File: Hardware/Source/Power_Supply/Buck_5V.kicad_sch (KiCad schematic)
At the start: 18 parts, among them U8 TPS54331DR

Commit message: update pcb flyback
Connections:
- net GND2: now also U8.7 (GND)
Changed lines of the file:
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@@
+	(wire
+		(pts
+			(xy 120.65 68.58) (xy 120.65 69.85)
+		)
+		(stroke
+			(width 0)
+			(type default)
+		)
+	)
 	(wire
 		(pts
@@
 		(pts
 			(xy 156.21 66.04) (xy 158.75 66.04)
+		)
+		(stroke
+			(width 0)
+			(type default)
+		)
+	)
+	(wire
+		(pts
+			(xy 130.81 68.58) (xy 120.65 68.58)
 		)
 		(stroke
@@
 					(unit 1)
 				)
+			)
+		)
+	)
+	(symbol
+		(lib_id "power:GND2")
+		(at 120.65 69.85 0)
+		(unit 1)
+		(exclude_from_sim no)
+		(in_bom yes)
+		(on_board yes)
+		(dnp no)
+		(fields_autoplaced yes)
+		(property "Reference" "#PWR027"
+			(at 120.65 76.2 0)
+			(effects
+				(font
+					(size 1.27 1.27)
+				)
+				(hide yes)
+			)
+		)
+		(property "Value" "GND2"
+			(at 120.65 74.93 0)
+			(effects
+				(font
+					(size 1.27 1.27)
+				)
+			)
+		)
+		(property "Footprint" ""
+			(at 120.65 69.85 0)
+			(effects
+				(font
+					(size 1.27 1.27)
+				)
+				(hide yes)
+			)
+		)
+		(property "Datasheet" ""
+			(at 120.65 69.85 0)
+			(effects
+				(font
+					(size 1.27 1.27)
+				)
+				(hide yes)
+			)
+		)
+		(property "Description" "Power symbol creates a global label with name \"GND2\" , ground"
+			(at 120.65 69.85 0)
+			(effects
+				(font
+					(size 1.27 1.27)
+				)
+				(hide yes)
+			)
+		)
+		(pin "1"
+		)
+		(instances
+			(project "Power_Supply"
+				(path "/5c8a7907-026b-4416-b231-5ef9f93b99e1/810061e0-77df-407e-a763-7d91437d6cce"
+					(reference "#PWR027")
+					(unit 1)
+				)

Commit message: update de sua sche
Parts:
- renumbered C25 to C45, C26 to C46, C27 to C47, C28 to C48, C29 to C49, C30 to C50, C31 to C51, C32 to C52, D4 to D11, L3 to L4, R19 to R28, R20 to R29, R21 to R30, R15 to R31, R16 to R32, R17 to R33, R18 to R34, U8 to U11
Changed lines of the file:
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@@
 		(on_board yes)
 		(dnp no)
-		(property "Reference" "C30"
+		(property "Reference" "C50"
 			(at 162.56 60.96 0)
 			(effects
@@
 		(pin "1"
 		)
-		(instances
-			(project ""
-				(path "/5c8a7907-026b-4416-b231-5ef9f93b99e1/810061e0-77df-407e-a763-7d91437d6cce"
-					(reference "C30")
-					(unit 1)
-				)
-			)
-		)
+		(instances)
 	)
 	(symbol
@@
 		(on_board yes)
 		(dnp no)
-		(property "Reference" "C32"
+		(property "Reference" "C52"
 			(at 220.726 77.47 90)
 			(effects
@@
 		(pin "2"
 		)
-		(instances
-			(project ""
-				(path "/5c8a7907-026b-4416-b231-5ef9f93b99e1/810061e0-77df-407e-a763-7d91437d6cce"
-					(reference "C32")
-					(unit 1)
-				)
-			)
-		)
+		(instances)
 	)
 	(symbol
@@
 		(on_board yes)
 		(dnp no)
-		(property "Reference" "C28"
+		(property "Reference" "C48"
 			(at 126.492 89.662 90)
 			(effects
@@
 		(pin "1"
 		)
-		(instances
-			(project ""
-				(path "/5c8a7907-026b-4416-b231-5ef9f93b99e1/810061e0-77df-407e-a763-7d91437d6cce"
-					(reference "C28")
-					(unit 1)
-				)
-			)
-		)
+		(instances)
 	)
 	(symbol
@@
 		(dnp no)
 		(fields_autoplaced yes)
-		(property "Reference" "U8"
+		(property "Reference" "U11"
 			(at 143.51 58.42 0)
 			(effects
@@
 		(pin "1"
 		)
-		(instances
-			(project ""
-				(path "/5c8a7907-026b-4416-b231-5ef9f93b99e1/810061e0-77df-407e-a763-7d91437d6cce"
-					(reference "U8")
-					(unit 1)
-				)
-			)
-		)
+		(instances)
 	)
 	(symbol
@@
 		(on_board yes)
 		(dnp no)
-		(property "Reference" "R21"
+		(property "Reference" "R30"
 			(at 106.934 94.996 90)
 			(effects
@@
 		(pin "2"
 		)
-		(instances
-			(project ""
-				(path "/5c8a7907-026b-4416-b231-5ef9f93b99e1/810061e0-77df-407e-a763-7d91437d6cce"
-					(reference "R21")
-					(unit 1)
-				)
-			)
-		)
+		(instances)
 	)
 	(symbol
@@
 		(on_board yes)
 		(dnp no)
-		(property "Reference" "R15"
+		(property "Reference" "R31"
 			(at 239.268 76.454 90)
 			(effects
@@
 		(pin "1"
 		)
-		(instances
-			(project ""
-				(path "/5c8a7907-026b-4416-b231-5ef9f93b99e1/810061e0-77df-407e-a763-7d91437d6cce"
-					(reference "R15")
-					(unit 1)
-				)
-			)
-		)
+		(instances)
 	)
 	(symbol
@@
 		(on_board yes)
 		(dnp no)
-		(property "Reference" "D4"
+		(property "Reference" "D11"
 			(at 172.466 76.708 90)
 			(effects
@@
 		(pin "1"
 		)
-		(instances
-			(project ""
-				(path "/5c8a7907-026b-4416-b231-5ef9f93b99e1/810061e0-77df-407e-a763-7d91437d6cce"
-					(reference "D4")
-					(unit 1)
-				)
-			)
-		)
+		(instances)
 	)
 	(symbol
@@
 		(on_board yes)
 		(dnp no)
-		(property "Reference" "C26"
+		(property "Reference" "C46"
 			(at 67.056 68.58 90)
 			(effects
@@
 		(pin "1"
 		)
-		(instances
-			(project ""
-				(path "/5c8a7907-026b-4416-b231-5ef9f93b99e1/810061e0-77df-407e-a763-7d91437d6cce"
-					(reference "C26")
-					(unit 1)
-				)
-			)
-		)
+		(instances)
 	)
 	(symbol
@@
 		(on_board yes)
 		(dnp no)
-		(property "Reference" "L3"
+		(property "Reference" "L4"
 			(at 182.88 66.04 0)
 			(effects
@@
 		(pin "2"
 		)
-		(instances
-			(project ""
-				(path "/5c8a7907-026b-4416-b231-5ef9f93b99e1/810061e0-77df-407e-a763-7d91437d6cce"
-					(reference "L3")
-					(unit 1)
-				)
-			)
-		)
+		(instances)
 	)
 	(symbol
@@
 		(on_board yes)
 		(dnp no)
-		(property "Reference" "C29"
+		(property "Reference" "C49"
 			(at 143.002 86.614 90)
 			(effects
@@
 		(pin "1"
 		)
-		(instances
-			(project ""
-				(path "/5c8a7907-026b-4416-b231-5ef9f93b99e1/810061e0-77df-407e-a763-7d91437d6cce"
-					(reference "C29")
-					(unit 1)
-				)
-			)
-		)
+		(instances)
 	)
 	(symbol
@@
 		(on_board yes)
 		(dnp no)
-		(property "Reference" "C31"
+		(property "Reference" "C51"
 			(at 201.93 77.47 90)
 			(effects
@@
 		(pin "2"
 		)
-		(instances
-			(project ""
-				(path "/5c8a7907-026b-4416-b231-5ef9f93b99e1/810061e0-77df-407e-a763-7d91437d6cce"
-					(reference "C31")
-					(unit 1)
-				)
-			)
-		)
+		(instances)
 	)
 	(symbol
@@
 		(on_board yes)
 		(dnp no)
-		(property "Reference" "R17"
+		(property "Reference" "R33"
 			(at 239.014 99.06 90)
 			(effects
@@
 		(pin "1"
 		)
-		(instances
-			(project ""
-				(path "/5c8a7907-026b-4416-b231-5ef9f93b99e1/810061e0-77df-407e-a763-7d91437d6cce"
-					(reference "R17")
-					(unit 1)
-				)
-			)
-		)
+		(instances)
 	)
 	(symbol
@@
 		(dnp no)
 		(fields_autoplaced yes)
-		(property "Reference" "#PWR019"
+		(property "Reference" "#PWR067"
 			(at 237.49 71.12 0)
 			(effects
@@
 		(pin "1"
 		)
-		(instances
-			(project ""
-				(path "/5c8a7907-026b-4416-b231-5ef9f93b99e1/810061e0-77df-407e-a763-7d91437d6cce"
-					(reference "#PWR019")
-					(unit 1)
-				)
-			)
-		)
+		(instances)
 	)
 	(symbol
@@
 		(on_board yes)
 		(dnp no)
-		(property "Reference" "R20"
+		(property "Reference" "R29"
 			(at 85.09 80.01 90)
 			(effects
@@
 		(pin "2"
 		)
-		(instances
-			(project ""
-				(path "/5c8a7907-026b-4416-b231-5ef9f93b99e1/810061e0-77df-407e-a763-7d91437d6cce"
-					(reference "R20")
-					(unit 1)
-				)
-			)
-		)
+		(instances)
 	)
 	(symbol
@@
 		(dnp no)
 		(fields_autoplaced yes)
-		(property "Reference" "#PWR014"
+		(property "Reference" "#PWR030"
 			(at 46.99 82.55 0)
 			(effects
@@
 		(pin "1"
 		)
-		(instances
-			(project ""
-				(path "/5c8a7907-026b-4416-b231-5ef9f93b99e1/810061e0-77df-407e-a763-7d91437d6cce"
-					(reference "#PWR014")
-					(unit 1)
-				)
-			)
-		)
+		(instances)
 	)
 	(symbol
@@
 		(on_board yes)
 		(dnp no)
-		(property "Reference" "R18"
+		(property "Reference" "R34"
 			(at 238.76 113.538 90)
 			(effects
@@
 		(pin "2"
 		)
-		(instances
-			(project ""
-				(path "/5c8a7907-026b-4416-b231-5ef9f93b99e1/810061e0-77df-407e-a763-7d91437d6cce"
-					(reference "R18")
-					(unit 1)
-				)
-			)
-		)
+		(instances)
 	)
 	(symbol
@@
 		(dnp no)
 		(fields_autoplaced yes)
-		(property "Reference" "#PWR013"
+		(property "Reference" "#PWR029"
 			(at 46.99 67.31 0)
 			(effects
@@
 		(pin "1"
 		)
-		(instances
-			(project ""
-				(path "/5c8a7907-026b-4416-b231-5ef9f93b99e1/810061e0-77df-407e-a763-7d91437d6cce"
-					(reference "#PWR013")
-					(unit 1)
-				)
-			)
-		)
+		(instances)
 	)
 	(symbol
@@
 		(on_board yes)
 		(dnp no)
-		(property "Reference" "C25"
+		(property "Reference" "C45"
 			(at 49.276 69.088 90)
 			(effects
@@
 		(pin "2"
 		)
-		(instances
-			(project ""
-				(path "/5c8a7907-026b-4416-b231-5ef9f93b99e1/810061e0-77df-407e-a763-7d91437d6cce"
-					(reference "C25")
-					(unit 1)
-				)
-			)
-		)
+		(instances)
 	)
 	(symbol
@@
 		(on_board yes)
 		(dnp no)
-		(property "Reference" "R16"
+		(property "Reference" "R32"
 			(at 239.014 87.63 90)
 			(effects
@@
 		(pin "2"
 		)
-		(instances
-			(project ""
-				(path "/5c8a7907-026b-4416-b231-5ef9f93b99e1/810061e0-77df-407e-a763-7d91437d6cce"
-					(reference "R16")
-					(unit 1)
-				)
-			)
-		)
+		(instances)
 	)
 	(symbol
@@
 		(on_board yes)
 		(dnp no)
-		(property "Reference" "C27"
+		(property "Reference" "C47"
 			(at 107.442 82.55 90)
 			(effects
@@
 		(pin "2"
 		)
-		(instances
-			(project ""
-				(path "/5c8a7907-026b-4416-b231-5ef9f93b99e1/810061e0-77df-407e-a763-7d91437d6cce"
-					(reference "C27")
-					(unit 1)
-				)
-			)
-		)
+		(instances)
 	)
 	(symbol
@@
 		(on_board yes)
 		(dnp no)
-		(property "Reference" "R19"
+		(property "Reference" "R28"
 			(at 85.598 68.58 90)
 			(effects
@@
 		(pin "1"
 		)
-		(instances
-			(project ""
-				(path "/5c8a7907-026b-4416-b231-5ef9f93b99e1/810061e0-77df-407e-a763-7d91437d6cce"
-					(reference "R19")
-					(unit 1)
-				)
-			)
-		)
+		(instances)
 	)
 )

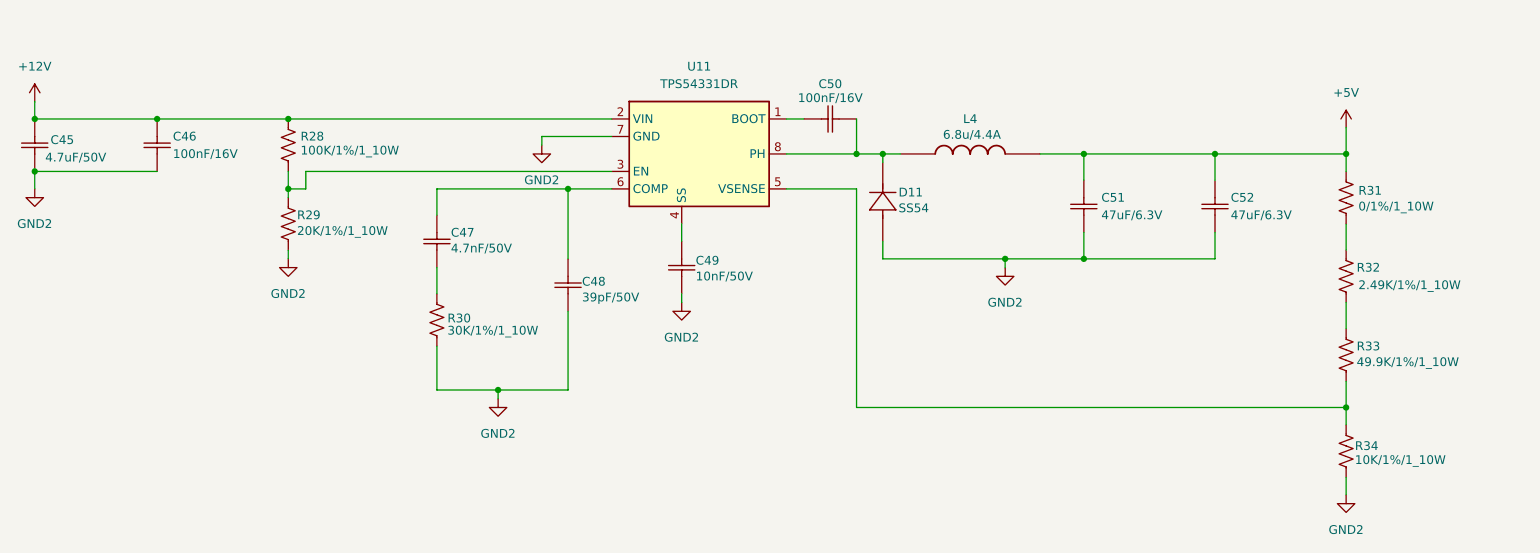
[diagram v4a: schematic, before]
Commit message: update flyback co 7V
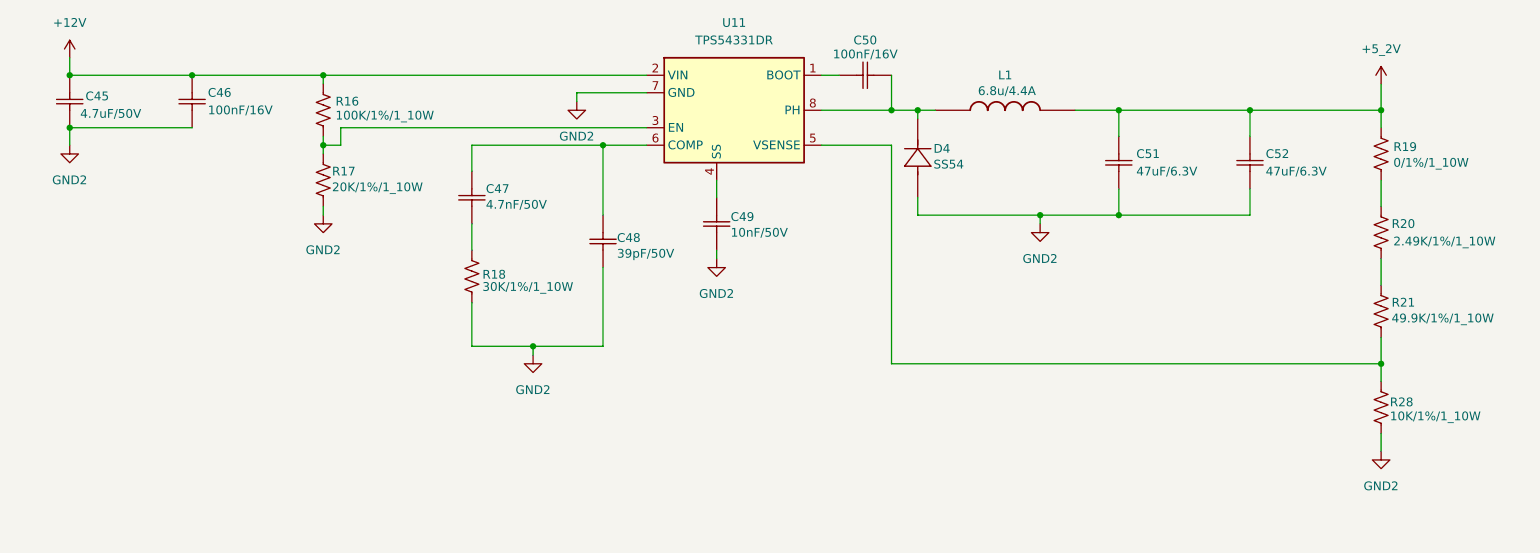
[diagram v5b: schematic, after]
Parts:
- removed D11: SS54, charge_battery_footprint_lib:D_SMA, symbol charge_battery_sym_lib:SS54
- removed L4: 6.8u/4.4A, charge_battery_footprint_lib:Inductor_6.8u_4.4A, symbol charge_battery_sym_lib:Inductor_6.8u_4.4A
- removed R28: 100K/1%/1_10W, charge_battery_footprint_lib:Res_0603, symbol charge_battery_sym_lib:Res_100K_0603_1%
- removed R29: 20K/1%/1_10W, charge_battery_footprint_lib:Res_0603, symbol charge_battery_sym_lib:Res_20K_0603_1%
- removed R30: 30K/1%/1_10W, charge_battery_footprint_lib:Res_0603, symbol charge_battery_sym_lib:Res_30K_0603_1%
- removed R31: 0/1%/1_10W, charge_battery_footprint_lib:Res_0603, symbol charge_battery_sym_lib:Res_0_0603_1%
- removed R32: 2.49K/1%/1_10W, charge_battery_footprint_lib:Res_0603, symbol charge_battery_sym_lib:Res_2.49K_0603_1%
- removed R33: 49.9K/1%/1_10W, charge_battery_footprint_lib:Res_0603, symbol charge_battery_sym_lib:Res_49.9K_0603_1%
- removed R34: 10K/1%/1_10W, charge_battery_footprint_lib:Res_0603, symbol charge_battery_sym_lib:Res_10K_0603_1%
- added D4: SS54, charge_battery_footprint_lib:D_SMA, symbol charge_battery_sym_lib:SS54
- added L1: 6.8u/4.4A, charge_battery_footprint_lib:Inductor_6.8u_4.4A, symbol charge_battery_sym_lib:Inductor_6.8u_4.4A
- added R16: 100K/1%/1_10W, charge_battery_footprint_lib:Res_0603, symbol charge_battery_sym_lib:Res_100K_0603_1%
- added R17: 20K/1%/1_10W, charge_battery_footprint_lib:Res_0603, symbol charge_battery_sym_lib:Res_20K_0603_1%
- added R18: 30K/1%/1_10W, charge_battery_footprint_lib:Res_0603, symbol charge_battery_sym_lib:Res_30K_0603_1%
- added R19: 0/1%/1_10W, charge_battery_footprint_lib:Res_0603, symbol charge_battery_sym_lib:Res_0_0603_1%
- added R20: 2.49K/1%/1_10W, charge_battery_footprint_lib:Res_0603, symbol charge_battery_sym_lib:Res_2.49K_0603_1%
- added R21: 49.9K/1%/1_10W, charge_battery_footprint_lib:Res_0603, symbol charge_battery_sym_lib:Res_49.9K_0603_1%
- added R28: 10K/1%/1_10W, charge_battery_footprint_lib:Res_0603, symbol charge_battery_sym_lib:Res_10K_0603_1%
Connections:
- net +12V: now also R16.2
- net GND2: now also D4.1 (A), R17.1, R18.1, R28.1
- net at C50.2, U11.8 (PH): now also D4.2 (K), L1.1
- net at U11.3 (EN): now also R16.1, R17.2
- net at U11.5 (VSENSE): now also R21.1, R28.2
- net at C47.1: now also R18.2
- net +5V renamed +5_2V
- net +5_2V: now also L1.2, R19.2
- new net: R20.1, R21.2
- new net: R19.1, R20.2

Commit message: Exported BOM List 4 boards
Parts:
- L1: Supply name (none) -> tme
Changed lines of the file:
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@@
 			)
 		)
-		(property "Description" " 4.5V to 28V Input, 3A, Synchronous Step-Down Converter with Eco-mode(tm)"
+		(property "Description" "4.5V to 28V Input, 3A, Synchronous Step-Down Converter with Eco-mode(tm)"
 			(at 148.082 93.472 0)
 			(effects
@@
 			(at 177.8 64.77 0)
 			(effects
+				(font
+					(size 1.27 1.27)
+				)
+				(hide yes)
+			)
+		)
+		(property "Supply name" "tme"
+			(at 177.8 64.77 0)
+			(effects
